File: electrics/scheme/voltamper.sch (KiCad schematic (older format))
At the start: 166 parts, among them K1 swd, K2 servo-1, K3 servo-2, P1 boot, P10 m3-hole, P11 m3-hole, P12 CONN_13X2, P2 boot, P3 -, P4 +, P5 work, P6 aux, P7 ref, P8 m3-hole, P9 m3-hole, Q1 bc857, Q2 bc847, Q3 bc857, Q4 bc847, Q5 irlml2244, Q6 bc847, Q7 bc847, Q8 bc847, SW1 btn-1, SW2 btn-2, U1 CRYSTAL-4PIN, U11 INA126, U12 SPARTAN-SIP-9007, U2 CP2102, U3 MICRO-USB-B, U4 MCP1703T-3302E/CB, U5 MCP1703T-3302E/CB, U6 NCP3063, U7 SPARTAN-SIP-9007, U8 NCP3063, U9 SPARTAN-SIP-9007

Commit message: About tot remove feedback buffer.
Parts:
- removed U? (x2): AD825, ~, symbol AD825
- added C44: 10n, ~, symbol C
- added R70, R71: 16, ~, symbol R
- added U10: LM258A, ~, symbol LM258A
- gave numbers to parts that had none: 37
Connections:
- wire segments 515 -> 549

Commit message: a
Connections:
- net labels added: GNDA
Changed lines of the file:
@@
 Wire Wire Line
 	18600 7050 18600 7150
-$Comp
-L GND #PWR090
-U 1 1 549B08B1
-P 18600 7150
-F 0 "#PWR090" H 18600 7150 30  0001 C CNN
-F 1 "GND" H 18600 7080 30  0001 C CNN
-F 2 "" H 18600 7150 60  0000 C CNN
-F 3 "" H 18600 7150 60  0000 C CNN
-	1    18600 7150
-	1    0    0    -1
-$EndComp
 Text Label 18300 5650 1    60   ~ 0
 v+
@@
 	17500 10550 17500 10650
 $Comp
-L GND #PWR092
-U 1 1 549B1EA2
-P 17500 10650
-F 0 "#PWR092" H 17500 10650 30  0001 C CNN
-F 1 "GND" H 17500 10580 30  0001 C CNN
-F 2 "" H 17500 10650 60  0000 C CNN
-F 3 "" H 17500 10650 60  0000 C CNN
-	1    17500 10650
-	1    0    0    -1
-$EndComp
-$Comp
 L C C23
 U 1 1 549B20CE
@@
 Wire Wire Line
 	18600 9150 18600 9300
-$Comp
-L GND #PWR093
-U 1 1 549B20D5
-P 18600 9300
-F 0 "#PWR093" H 18600 9300 30  0001 C CNN
-F 1 "GND" H 18600 9230 30  0001 C CNN
-F 2 "" H 18600 9300 60  0000 C CNN
-F 3 "" H 18600 9300 60  0000 C CNN
-	1    18600 9300
-	1    0    0    -1
-$EndComp
 Wire Wire Line
 	18600 8750 18600 8600
@@
 	22750 15600 22750 17100
 Connection ~ 22750 17100
+$Comp
+L GNDA #PWR?
+U 1 1 549D197B
+P 17500 10650
+F 0 "#PWR?" H 17500 10650 40  0001 C CNN
+F 1 "GNDA" H 17500 10580 40  0000 C CNN
+F 2 "" H 17500 10650 60  0000 C CNN
+F 3 "" H 17500 10650 60  0000 C CNN
+	1    17500 10650
+	1    0    0    -1
+$EndComp
+$Comp
+L GNDA #PWR?
+U 1 1 549D1992
+P 18600 9300
+F 0 "#PWR?" H 18600 9300 40  0001 C CNN
+F 1 "GNDA" H 18600 9230 40  0000 C CNN
+F 2 "" H 18600 9300 60  0000 C CNN
+F 3 "" H 18600 9300 60  0000 C CNN
+	1    18600 9300
+	1    0    0    -1
+$EndComp
+$Comp
+L GNDA #PWR?
+U 1 1 549D19A2
+P 18600 7150
+F 0 "#PWR?" H 18600 7150 40  0001 C CNN
+F 1 "GNDA" H 18600 7080 40  0000 C CNN
+F 2 "" H 18600 7150 60  0000 C CNN
+F 3 "" H 18600 7150 60  0000 C CNN
+	1    18600 7150
+	1    0    0    -1
+$EndComp
 $EndSCHEMATC

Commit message: a
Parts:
- removed C12, C27, C37: 10n, ~, symbol C
- removed C38, C39: 4u7, ~, symbol C
- removed R22, R35: 10k 0.1%, ~, symbol R
- removed R63, R64: 16, ~, symbol R
- removed R65, R66: 1k 0.1%, ~, symbol R
- added R?: 10k 0.1%, ~, symbol R
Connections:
- net labels added: f+, f-
- wire segments 549 -> 526
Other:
- moved on the sheet: R17, R60

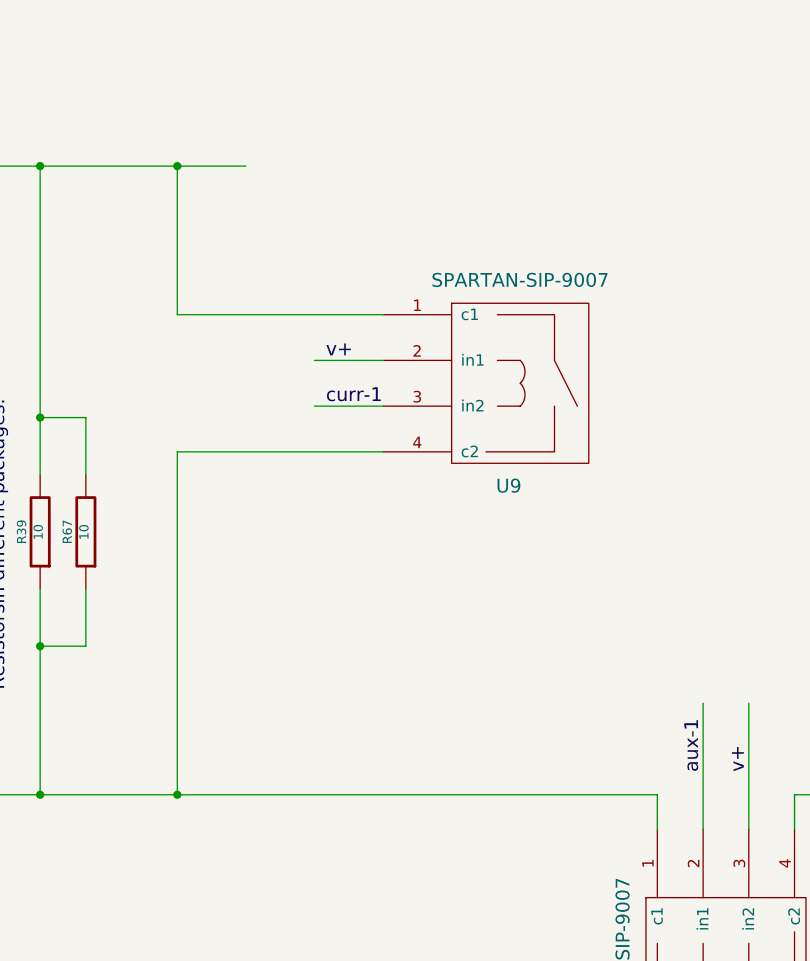
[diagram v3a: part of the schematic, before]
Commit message: Very first modelling it works but it doesn't show any plots.
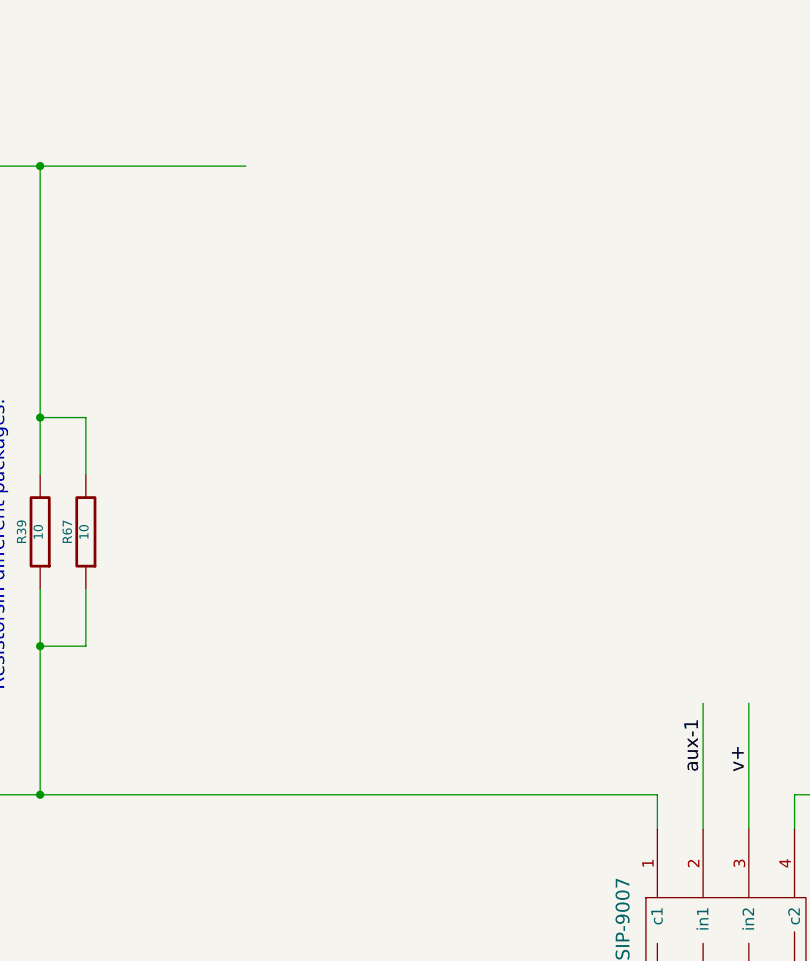
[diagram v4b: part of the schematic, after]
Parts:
- removed U9: SPARTAN-SIP-9007, ~, symbol SPARTAN-SIP-9007
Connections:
- wire segments 526 -> 520
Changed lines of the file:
@@
 AVdd
-$Comp
-L SPARTAN-SIP-9007 U9
-U 1 1 5485DF9C
-P 24200 15300
-F 0 "U9" H 24200 14850 60  0000 C CNN
-F 1 "SPARTAN-SIP-9007" H 24250 15750 60  0000 C CNN
-F 2 "~" H 24200 15300 60  0000 C CNN
-F 3 "~" H 24200 15300 60  0000 C CNN
-	1    24200 15300
-	1    0    0    -1
-$EndComp
-Wire Wire Line
-	22750 15000 23650 15000
-Wire Wire Line
-	23650 15400 23350 15400
-Wire Wire Line
-	23650 15200 23350 15200
 $Comp
 L SPARTAN-SIP-9007 U7
@@
 Wire Wire Line
 	23450 9800 23450 10050
-Text Label 23400 15400 0    60   ~ 0
-curr-1
 Text Label 23250 9850 3    60   ~ 0
 volt-1
@@
 Text Label 23450 9850 3    60   ~ 0
 v+
-Text Label 23400 15200 0    60   ~ 0
-v+
 Text Label 25250 17000 1    60   ~ 0
 v+
@@
 	22150 16200 22150 17100
 Connection ~ 22150 17100
-Wire Wire Line
-	22750 15000 22750 14350
-Connection ~ 22750 14350
 $Comp
 L LM258A U10
@@
 	19150 17600 19150 17300
 Connection ~ 19150 17300
-Wire Wire Line
-	22750 15600 23650 15600
-Wire Wire Line
-	22750 15600 22750 17100
-Connection ~ 22750 17100
 $Comp
 L GNDA #PWR?

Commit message: a
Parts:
- removed D8: 1N5819, ~, symbol DIODESCH
- removed Q7: bc847, ~, symbol NPN
- removed R26: 1k, ~, symbol R
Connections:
- net labels removed: curr-1
- wire segments 520 -> 513
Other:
- moved on the sheet: D9, Q8, R27
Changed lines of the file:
@@
 Sheet 1 1
 Title ""
-Date "1 jan 2015"
+Date "2 jan 2015"
 Rev ""
 Comp ""
@@
 volt-en
 $Comp
-L NPN Q7
-U 1 1 548613CB
-P 11800 18900
-F 0 "Q7" H 11800 18750 50  0000 R CNN
-F 1 "bc847" H 11800 19050 50  0000 R CNN
-F 2 "~" H 11800 18900 60  0000 C CNN
-F 3 "~" H 11800 18900 60  0000 C CNN
-	1    11800 18900
-	1    0    0    -1
-$EndComp
-$Comp
-L R R26
-U 1 1 548613D1
-P 11150 18900
-F 0 "R26" V 11230 18900 40  0000 C CNN
-F 1 "1k" V 11157 18901 40  0000 C CNN
-F 2 "~" V 11080 18900 30  0000 C CNN
-F 3 "~" H 11150 18900 30  0000 C CNN
-	1    11150 18900
-	0    -1   -1   0
-$EndComp
-Wire Wire Line
-	11600 18900 11400 18900
-Wire Wire Line
-	11900 18700 11900 18200
-Wire Wire Line
-	11900 19100 11900 19350
-$Comp
-L GND #PWR055
-U 1 1 548613DA
-P 11900 19350
-F 0 "#PWR055" H 11900 19350 30  0001 C CNN
-F 1 "GND" H 11900 19280 30  0001 C CNN
-F 2 "" H 11900 19350 60  0000 C CNN
-F 3 "" H 11900 19350 60  0000 C CNN
-	1    11900 19350
-	1    0    0    -1
-$EndComp
-Wire Wire Line
-	10900 18900 10450 18900
-Text Label 11900 18550 1    60   ~ 0
-curr-1
-Wire Wire Line
-	11900 17300 11900 18050
-Text Label 11900 17450 1    60   ~ 0
-v+
-Text Label 10500 18900 0    60   ~ 0
-curr-en
-$Comp
 L NPN Q8
 U 1 1 548615B1
-P 13550 18900
-F 0 "Q8" H 13550 18750 50  0000 R CNN
-F 1 "bc847" H 13550 19050 50  0000 R CNN
-F 2 "~" H 13550 18900 60  0000 C CNN
-F 3 "~" H 13550 18900 60  0000 C CNN
-	1    13550 18900
+P 12100 18900
+F 0 "Q8" H 12100 18750 50  0000 R CNN
+F 1 "bc847" H 12100 19050 50  0000 R CNN
+F 2 "~" H 12100 18900 60  0000 C CNN
+F 3 "~" H 12100 18900 60  0000 C CNN
+	1    12100 18900
 	1    0    0    -1
 $EndComp
@@
 L R R27
 U 1 1 548615B7
-P 12900 18900
-F 0 "R27" V 12980 18900 40  0000 C CNN
-F 1 "1k" V 12907 18901 40  0000 C CNN
-F 2 "~" V 12830 18900 30  0000 C CNN
-F 3 "~" H 12900 18900 30  0000 C CNN
-	1    12900 18900
+P 11450 18900
+F 0 "R27" V 11530 18900 40  0000 C CNN
+F 1 "1k" V 11457 18901 40  0000 C CNN
+F 2 "~" V 11380 18900 30  0000 C CNN
+F 3 "~" H 11450 18900 30  0000 C CNN
+	1    11450 18900
 	0    -1   -1   0
 $EndComp
 Wire Wire Line
-	13350 18900 13150 18900
-Wire Wire Line
-	13650 18700 13650 18200
-Wire Wire Line
-	13650 19100 13650 19350
+	11900 18900 11700 18900
+Wire Wire Line
+	12200 18700 12200 18200
+Wire Wire Line
+	12200 19100 12200 19350
 $Comp
 L GND #PWR056
 U 1 1 548615C0
-P 13650 19350
-F 0 "#PWR056" H 13650 19350 30  0001 C CNN
-F 1 "GND" H 13650 19280 30  0001 C CNN
-F 2 "" H 13650 19350 60  0000 C CNN
-F 3 "" H 13650 19350 60  0000 C CNN
-	1    13650 19350
-	1    0    0    -1
-$EndComp
-Wire Wire Line
-	12650 18900 12200 18900
-Text Label 13650 18550 1    60   ~ 0
+P 12200 19350
+F 0 "#PWR056" H 12200 19350 30  0001 C CNN
+F 1 "GND" H 12200 19280 30  0001 C CNN
+F 2 "" H 12200 19350 60  0000 C CNN
+F 3 "" H 12200 19350 60  0000 C CNN
+	1    12200 19350
+	1    0    0    -1
+$EndComp
+Wire Wire Line
+	11200 18900 10750 18900
+Text Label 12200 18550 1    60   ~ 0
 aux-1
 Wire Wire Line
-	13650 17300 13650 18050
-Text Label 13650 17450 1    60   ~ 0
+	12200 17300 12200 18050
+Text Label 12200 17450 1    60   ~ 0
 v+
-Text Label 12250 18900 0    60   ~ 0
+Text Label 10800 18900 0    60   ~ 0
 aux-en
 $Comp
@@
 Connection ~ 10100 18350
 $Comp
-L DIODESCH D8
-U 1 1 5485E6E8
-P 12100 18150
-F 0 "D8" H 12100 18250 40  0000 C CNN
-F 1 "1N5819" H 12100 18050 40  0000 C CNN
-F 2 "~" H 12100 18150 60  0000 C CNN
-F 3 "~" H 12100 18150 60  0000 C CNN
-	1    12100 18150
-	0    -1   -1   0
-$EndComp
-Wire Wire Line
-	12100 17950 11900 17950
-Connection ~ 11900 17950
-Wire Wire Line
-	12100 18350 11900 18350
-Connection ~ 11900 18350
-$Comp
 L DIODESCH D9
 U 1 1 5485EACA
-P 13850 18150
-F 0 "D9" H 13850 18250 40  0000 C CNN
-F 1 "1N5819" H 13850 18050 40  0000 C CNN
-F 2 "~" H 13850 18150 60  0000 C CNN
-F 3 "~" H 13850 18150 60  0000 C CNN
-	1    13850 18150
+P 12400 18150
+F 0 "D9" H 12400 18250 40  0000 C CNN
+F 1 "1N5819" H 12400 18050 40  0000 C CNN
+F 2 "~" H 12400 18150 60  0000 C CNN
+F 3 "~" H 12400 18150 60  0000 C CNN
+	1    12400 18150
 	0    -1   -1   0
 $EndComp
 Wire Wire Line
-	13850 17950 13650 17950
-Connection ~ 13650 17950
-Wire Wire Line
-	13850 18350 13650 18350
-Connection ~ 13650 18350
+	12400 17950 12200 17950
+Connection ~ 12200 17950
+Wire Wire Line
+	12400 18350 12200 18350
+Connection ~ 12200 18350
 $Comp
 L LED D10

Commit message: almost adjusted original scheme. Modifying input op amp is left to do.
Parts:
- removed C42, C43: 4u7, ~, symbol C
- removed C44: 10n, ~, symbol C
- removed R68, R69: 16, ~, symbol R
- removed R?: 10k 0.1%, ~, symbol R
- removed unit 2 of U10
- removed U15: AD825, ~, symbol AD825
- added C12: 30n, ~, symbol C
- added D4: 1N5819, ~, symbol DIODESCH
- added Q7: bc847, ~, symbol NPN
- added R22: 1k, ~, symbol R
- added R26: 120k, ~, symbol R
- added R35: 410, ~, symbol R
- added U9: SPARTAN-SIP-9007, ~, symbol SPARTAN-SIP-9007
- C18: value 10n -> 1n
- R17: value 10k 0.1% -> 120k
- R58, R59: value 10k 0.1% -> 410
- R60: value 10k 0.1% -> 0
- U10: value LM258A -> ADA4000
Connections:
- net labels added: curr-1
- net labels removed: intermediate, pre-eaux
- wire segments 513 -> 498
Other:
- moved on the sheet: C18, C20, C23, C25, C26, C30, C34, C35, C41, K2, K3, P5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

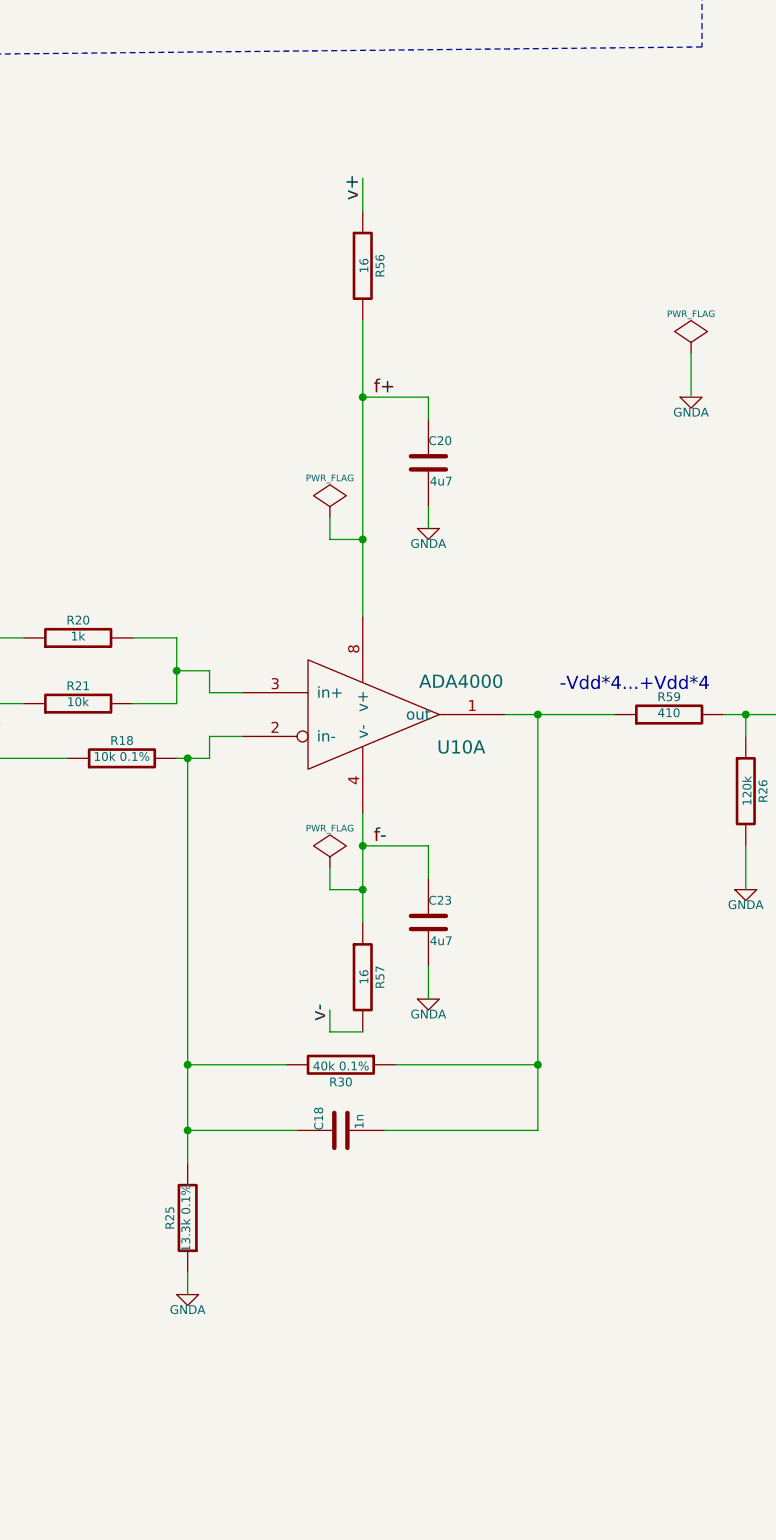
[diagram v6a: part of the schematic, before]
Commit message: Made footprint for opa551.
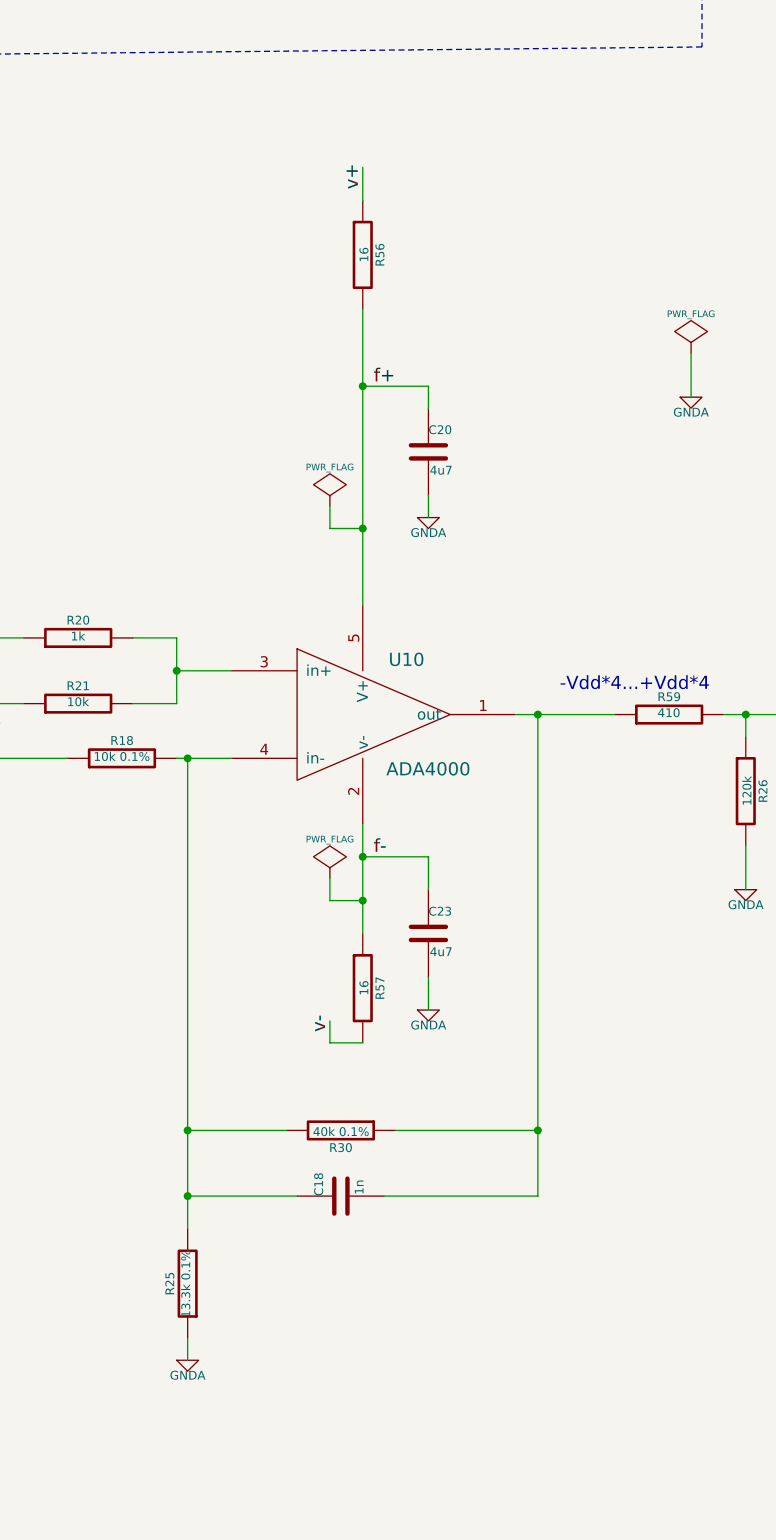
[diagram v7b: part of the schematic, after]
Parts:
- removed U10: ADA4000, ~, symbol LM258A
- added U10: ADA4000, ~, symbol ADA4000
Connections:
- wire segments 498 -> 494
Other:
- moved on the sheet: C18, C20, C23, R25, R30, R56, R57

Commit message: a
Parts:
- added D6: 1N5819, ~, symbol DIODESCH
- added Q9: bc847, ~, symbol NPN
- added R63: 1k, ~, symbol R
- added U15: SPARTAN-SIP-9007, ~, symbol SPARTAN-SIP-9007
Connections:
- net labels added: aux-pre, short-1, short-en
- wire segments 494 -> 508
- no-connect marks 26 -> 25
